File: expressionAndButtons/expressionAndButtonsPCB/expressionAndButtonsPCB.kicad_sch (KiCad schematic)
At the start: 62 parts, among them J1 Alimentazione, J2 Input comandi, J3 OUTPUT C, J4 OUTPUT I, J5 OUTPUT III, J6 INPUT C-I-III, U2 ProMicro

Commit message: Progresso bottoniera
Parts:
- removed J2: Input comandi, TerminalBlock_Phoenix:TerminalBlock_Phoenix_MKDS-1,5-16_1x16_P5.00mm_Horizontal, symbol Connector_Generic:Conn_01x16
- removed J3: OUTPUT C, TerminalBlock_Phoenix:TerminalBlock_Phoenix_MKDS-1,5-16_1x16_P5.00mm_Horizontal, symbol Connector_Generic:Conn_01x16
- added J2, J3: Conn_01x12, TerminalBlock_Phoenix:TerminalBlock_Phoenix_MPT-0,5-12-2.54_1x12_P2.54mm_Horizontal, symbol Connector_Generic:Conn_01x12
- added J7, J8: Conn_01x04, TerminalBlock_Phoenix:TerminalBlock_Phoenix_MPT-0,5-4-2.54_1x04_P2.54mm_Horizontal, symbol Connector_Generic:Conn_01x04
- J4, J5: footprint TerminalBlock_Phoenix:TerminalBlock_Phoenix_MKDS-1,5-9-5.08_1x09_P5.08mm_Horizontal -> TerminalBlock_Phoenix:TerminalBlock_Phoenix_MPT-0,5-9-2.54_1x09_P2.54mm_Horizontal
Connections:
- net at IN1.5 (D6), R7.1: now also J2.7 (Pin_7)
- net at Cresc1.10 (~{SRCLR}), Cresc1.13 (~{OE}), Cresc1.16 (VCC)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: now also Cresc2.10 (~{SRCLR}), Cresc2.13 (~{OE}), Cresc2.16 (VCC)
- net at IN1.11 (D0), R1.1: now also J2.1 (Pin_1)
- net at IN2.12 (D1), R10.1: now also J2.10 (Pin_10)
- net at IN2.13 (D2), R11.1: now also J2.11 (Pin_11)
- net at IN2.14 (D3), R12.1: now also J2.12 (Pin_12)
- net at IN2.3 (D4), R13.1: now also J7.1 (Pin_1)
- net at IN2.4 (D5), R14.1: now also J7.2 (Pin_2)
- net at IN2.5 (D6), R15.1: now also J7.3 (Pin_3)
- net at IN2.6 (D7), R16.1: now also J7.4 (Pin_4)
- net at IN1.12 (D1), R2.1: now also J2.2 (Pin_2)
- net at IN1.13 (D2), R3.1: now also J2.3 (Pin_3)
- net at IN1.14 (D3), R4.1: now also J2.4 (Pin_4)
- net at IN1.3 (D4), R5.1: now also J2.5 (Pin_5)
- net at IN1.4 (D5), R6.1: now also J2.6 (Pin_6)
- net at IN1.6 (D7), R8.1: now also J2.8 (Pin_8)
- net at IN2.11 (D0), R9.1: now also J2.9 (Pin_9)
- net at R17.2: now also J3.1 (Pin_1)
- net at R26.2: now also J3.10 (Pin_10)
- net at R27.2: now also J3.11 (Pin_11)
- net at R28.2: now also J3.12 (Pin_12)
- net at R29.2: now also J8.1 (Pin_1)
- net at R30.2: now also J8.2 (Pin_2)
- net at R31.2: now also J8.3 (Pin_3)
- net at R32.2: now also J8.4 (Pin_4)
- net at R18.2: now also J3.2 (Pin_2)
- net at R19.2: now also J3.3 (Pin_3)
- net at R20.2: now also J3.4 (Pin_4)
- net at R21.2: now also J3.5 (Pin_5)
- net at R22.2: now also J3.6 (Pin_6)
- net at R23.2: now also J3.7 (Pin_7)
- net at R24.2: now also J3.8 (Pin_8)
- net at R25.2: now also J3.9 (Pin_9)
- net at IN1.7 (~{Q7}): no longer IN2.10 (DS)
- net at IN1.9 (Q7): now also IN2.10 (DS)

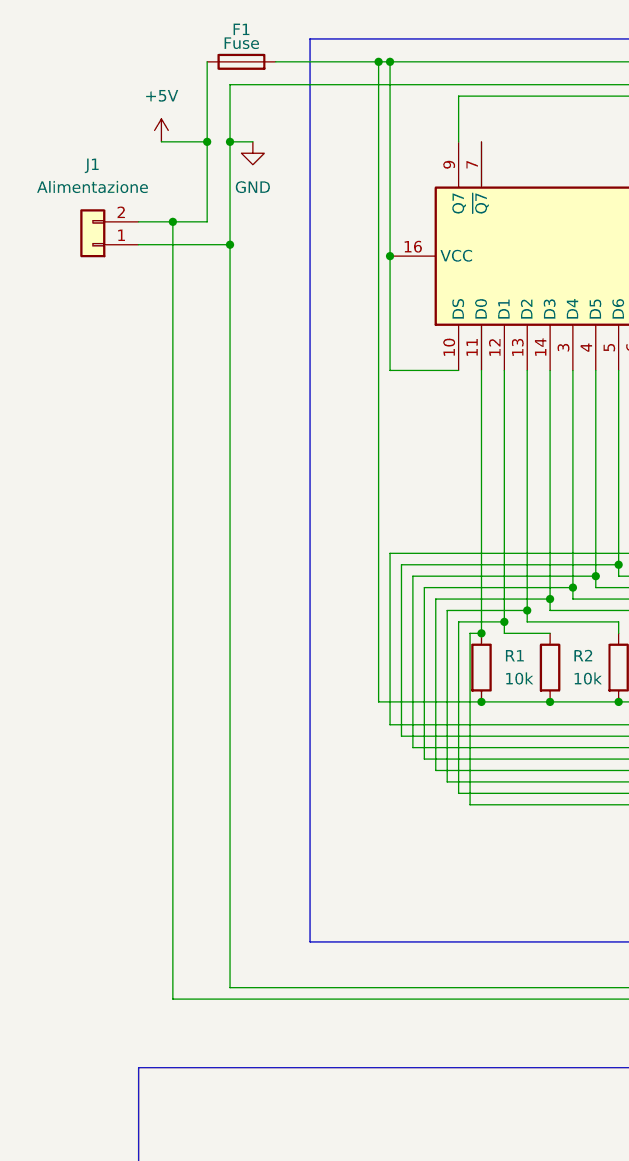
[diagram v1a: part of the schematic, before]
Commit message: First version buttons
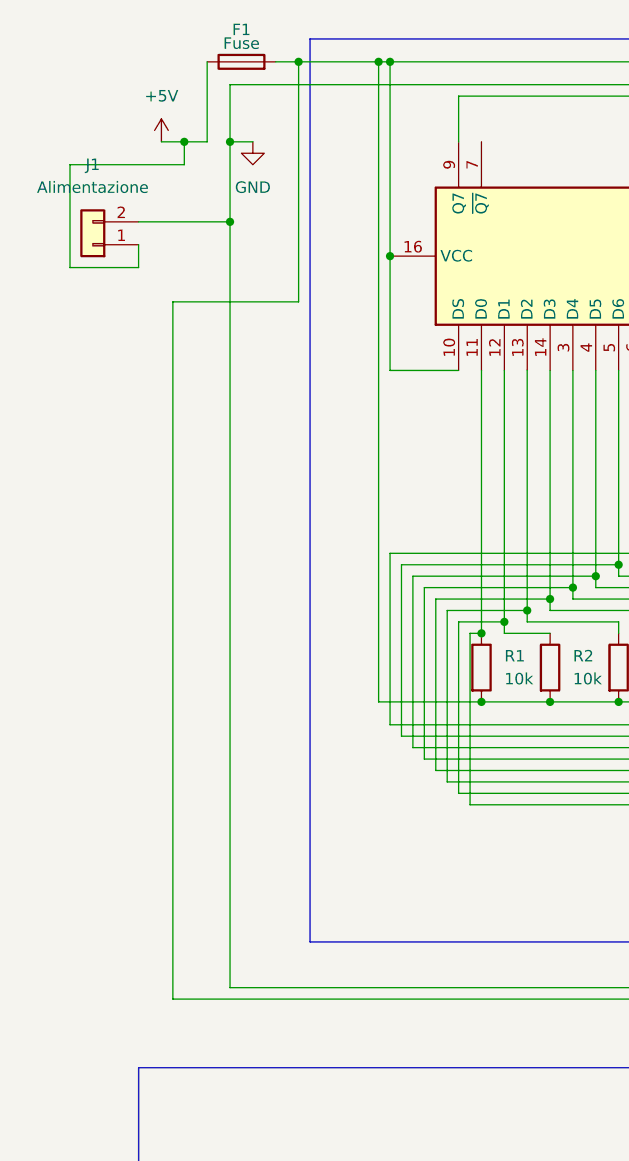
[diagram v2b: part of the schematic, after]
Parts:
- J6: footprint TerminalBlock_Phoenix:TerminalBlock_Phoenix_MKDS-1,5-5-5.08_1x05_P5.08mm_Horizontal -> TerminalBlock_Phoenix:TerminalBlock_Phoenix_MPT-0,5-5-2.54_1x05_P2.54mm_Horizontal
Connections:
- net +5V: now also J1.1 (Pin_1); no longer J1.2 (Pin_2), J6.4 (Pin_4)
- net GND: now also J1.2 (Pin_2); no longer J1.1 (Pin_1)
- net at Cresc1.10 (~{SRCLR}), Cresc1.13 (~{OE}), Cresc1.16 (VCC)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: now also J6.4 (Pin_4)
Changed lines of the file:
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@@
 	)
 	(junction
-		(at 29.21 34.29)
-		(diameter 0)
-		(color 0 0 0 0)
-	)
-	(junction
-		(at 35.56 36.83)
-		(diameter 0)
-		(color 0 0 0 0)
-	)
-	(junction
 		(at 111.76 16.51)
 		(diameter 0)
@@
 	)
 	(junction
-		(at 33.02 25.4)
-		(diameter 0)
-		(color 0 0 0 0)
-	)
-	(junction
 		(at 66.04 78.74)
 		(diameter 0)
@@
 	)
 	(junction
+		(at 35.56 34.29)
+		(diameter 0)
+		(color 0 0 0 0)
+	)
+	(junction
 		(at 236.22 116.84)
 		(diameter 0)
@@
 	)
 	(junction
+		(at 30.48 25.4)
+		(diameter 0)
+		(color 0 0 0 0)
+	)
+	(junction
 		(at 81.28 71.12)
 		(diameter 0)
@@
 	)
 	(junction
+		(at 43.18 16.51)
+		(diameter 0)
+		(color 0 0 0 0)
+	)
+	(junction
 		(at 132.08 87.63)
 		(diameter 0)
@@
 	(wire
 		(pts
+			(xy 43.18 43.18) (xy 43.18 16.51)
+		)
+		(stroke
+			(width 0)
+			(type default)
+		)
+	)
+	(wire
+		(pts
 			(xy 345.44 158.75) (xy 345.44 148.59)
 		)
@@
 	(wire
 		(pts
-			(xy 35.56 36.83) (xy 35.56 25.4)
+			(xy 254 72.39) (xy 254 83.82)
 		)
 		(stroke
@@
 	(wire
 		(pts
-			(xy 254 72.39) (xy 254 83.82)
+			(xy 259.08 154.94) (xy 278.13 154.94)
 		)
 		(stroke
@@
 	(wire
 		(pts
-			(xy 259.08 154.94) (xy 278.13 154.94)
+			(xy 147.32 87.63) (xy 154.94 87.63)
 		)
 		(stroke
@@
 	(wire
 		(pts
-			(xy 147.32 87.63) (xy 154.94 87.63)
+			(xy 312.42 83.82) (xy 312.42 77.47)
 		)
 		(stroke
@@
 	(wire
 		(pts
-			(xy 312.42 83.82) (xy 312.42 77.47)
+			(xy 30.48 27.94) (xy 17.78 27.94)
 		)
 		(stroke
@@
 	(wire
 		(pts
+			(xy 43.18 16.51) (xy 52.07 16.51)
+		)
+		(stroke
+			(width 0)
+			(type default)
+		)
+	)
+	(wire
+		(pts
 			(xy 341.63 184.15) (xy 354.33 184.15)
 		)
@@
 	(wire
 		(pts
+			(xy 17.78 39.37) (xy 25.4 39.37)
+		)
+		(stroke
+			(width 0)
+			(type default)
+		)
+	)
+	(wire
+		(pts
 			(xy 274.32 123.19) (xy 237.49 123.19)
 		)
@@
 	(wire
 		(pts
+			(xy 29.21 43.18) (xy 43.18 43.18)
+		)
+		(stroke
+			(width 0)
+			(type default)
+		)
+	)
+	(wire
+		(pts
 			(xy 73.66 76.2) (xy 93.98 76.2)
 		)
@@
 	(wire
 		(pts
-			(xy 91.44 50.8) (xy 91.44 57.15)
+			(xy 30.48 25.4) (xy 33.02 25.4)
 		)
 		(stroke
@@
 	(wire
 		(pts
-			(xy 369.57 184.15) (xy 389.89 184.15)
+			(xy 91.44 50.8) (xy 91.44 57.15)
 		)
 		(stroke
@@
 	(wire
 		(pts
-			(xy 360.68 59.69) (xy 360.68 64.77)
+			(xy 369.57 184.15) (xy 389.89 184.15)
 		)
 		(stroke
@@
 	(wire
 		(pts
-			(xy 53.34 16.51) (xy 53.34 38.1)
+			(xy 360.68 59.69) (xy 360.68 64.77)
 		)
 		(stroke
@@
 	(wire
 		(pts
-			(xy 25.4 34.29) (xy 29.21 34.29)
+			(xy 53.34 16.51) (xy 53.34 38.1)
 		)
 		(stroke
@@
 	(wire
 		(pts
-			(xy 25.4 36.83) (xy 35.56 36.83)
+			(xy 29.21 43.18) (xy 29.21 120.65)
 		)
 		(stroke
@@
 	(wire
 		(pts
+			(xy 25.4 39.37) (xy 25.4 36.83)
+		)
+		(stroke
+			(width 0)
+			(type default)
+		)
+	)
+	(wire
+		(pts
 			(xy 127 96.52) (xy 158.75 96.52)
 		)
@@
 	(wire
 		(pts
-			(xy 27.94 25.4) (xy 33.02 25.4)
+			(xy 27.94 25.4) (xy 30.48 25.4)
 		)
 		(stroke
@@
 	(wire
 		(pts
-			(xy 33.02 25.4) (xy 33.02 34.29)
-		)
-		(stroke
-			(width 0)
-			(type default)
-		)
-	)
-	(wire
-		(pts
 			(xy 59.69 77.47) (xy 68.58 77.47)
 		)
@@
 	(wire
 		(pts
+			(xy 30.48 25.4) (xy 30.48 27.94)
+		)
+		(stroke
+			(width 0)
+			(type default)
+		)
+	)
+	(wire
+		(pts
 			(xy 57.15 74.93) (xy 73.66 74.93)
 		)
@@
 	(wire
 		(pts
-			(xy 35.56 119.38) (xy 35.56 36.83)
+			(xy 35.56 25.4) (xy 35.56 34.29)
 		)
 		(stroke
@@
 	(wire
 		(pts
-			(xy 29.21 34.29) (xy 29.21 120.65)
-		)
-		(stroke
-			(width 0)
-			(type default)
-		)
-	)
-	(wire
-		(pts
 			(xy 60.96 20.32) (xy 110.49 20.32)
 		)
@@
 	(wire
 		(pts
-			(xy 40.64 16.51) (xy 52.07 16.51)
+			(xy 40.64 16.51) (xy 43.18 16.51)
 		)
 		(stroke
@@
 	(wire
 		(pts
+			(xy 35.56 34.29) (xy 35.56 119.38)
+		)
+		(stroke
+			(width 0)
+			(type default)
+		)
+	)
+	(wire
+		(pts
 			(xy 160.02 52.07) (xy 152.4 52.07)
 		)
@@
 	(wire
 		(pts
-			(xy 29.21 34.29) (xy 33.02 34.29)
+			(xy 17.78 27.94) (xy 17.78 39.37)
 		)
 		(stroke
@@
 	(wire
 		(pts
+			(xy 25.4 34.29) (xy 35.56 34.29)
+		)
+		(stroke
+			(width 0)
+			(type default)
+		)
+	)
+	(wire
+		(pts
 			(xy 287.02 153.67) (xy 287.02 163.83)
 		)
@@
 			)
 		)
-		(property "Footprint" "TerminalBlock_Phoenix:TerminalBlock_Phoenix_MKDS-1,5-5-5.08_1x05_P5.08mm_Horizontal"
+		(property "Footprint" "TerminalBlock_Phoenix:TerminalBlock_Phoenix_MPT-0,5-5-2.54_1x05_P2.54mm_Horizontal"
 			(at 139.7 231.14 0)
 			(effects

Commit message: update
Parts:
- J1: footprint TerminalBlock_Phoenix:TerminalBlock_Phoenix_MKDS-1,5-2-5.08_1x02_P5.08mm_Horizontal -> TerminalBlock_Phoenix:TerminalBlock_Phoenix_MPT-0,5-2-2.54_1x02_P2.54mm_Horizontal
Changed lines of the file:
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@@
 			)
 		)
-		(property "Footprint" "TerminalBlock_Phoenix:TerminalBlock_Phoenix_MKDS-1,5-2-5.08_1x02_P5.08mm_Horizontal"
+		(property "Footprint" "TerminalBlock_Phoenix:TerminalBlock_Phoenix_MPT-0,5-2-2.54_1x02_P2.54mm_Horizontal"
 			(at 20.32 36.83 0)
 			(effects

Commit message: problem fix
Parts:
- removed J2, J3: Conn_01x12, TerminalBlock_Phoenix:TerminalBlock_Phoenix_MPT-0,5-12-2.54_1x12_P2.54mm_Horizontal, symbol Connector_Generic:Conn_01x12
- removed J7, J8: Conn_01x04, TerminalBlock_Phoenix:TerminalBlock_Phoenix_MPT-0,5-4-2.54_1x04_P2.54mm_Horizontal, symbol Connector_Generic:Conn_01x04
- added J2, J7: Conn_01x06, TerminalBlock_Phoenix:TerminalBlock_Phoenix_MPT-0,5-6-2.54_1x06_P2.54mm_Horizontal, symbol Connector_Generic:Conn_01x06
- added J3, J9: Conn_01x10, TerminalBlock_Phoenix:TerminalBlock_Phoenix_MPT-0,5-10-2.54_1x10_P2.54mm_Horizontal, symbol Connector_Generic:Conn_01x10
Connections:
- net GND: now also Cresc1.13 (~{OE}), Cresc2.13 (~{OE}), E1.13 (~{OE}), E2.13 (~{OE})
- net at IN1.5 (D6), R7.1: now also J9.7 (Pin_7)
- net at Cresc1.10 (~{SRCLR}), Cresc1.16 (VCC), Cresc2.10 (~{SRCLR})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: no longer Cresc1.13 (~{OE}), Cresc2.13 (~{OE}), E1.13 (~{OE}), E2.13 (~{OE})
- net at IN2.12 (D1), R10.1: now also J9.10 (Pin_10)
- net at R30.2: now also J7.4 (Pin_4)
- net at R22.2: now also J3.6 (Pin_6)
- net at R17.2: now also J3.1 (Pin_1)
- net at R26.2: now also J3.10 (Pin_10)
- net at R27.2: now also J7.1 (Pin_1)
- net at R28.2: now also J7.2 (Pin_2)
- net at R18.2: now also J3.2 (Pin_2)
- net at R19.2: now also J3.3 (Pin_3)
- net at R20.2: now also J3.4 (Pin_4)
- net at R21.2: now also J3.5 (Pin_5)
- net at R23.2: now also J3.7 (Pin_7)
- net at R24.2: now also J3.8 (Pin_8)
- net at R25.2: now also J3.9 (Pin_9)
- net at IN2.3 (D4), R13.1: now also J2.3 (Pin_3)
- net at IN1.12 (D1), R2.1: now also J9.2 (Pin_2)
- net at IN2.4 (D5), R14.1: now also J2.4 (Pin_4)
- net at IN2.14 (D3), R12.1: now also J2.2 (Pin_2)
- net at IN2.6 (D7), R16.1: now also J2.6 (Pin_6)
- net at IN2.5 (D6), R15.1: now also J2.5 (Pin_5)
- net at R32.2: now also J7.6 (Pin_6)
- net at IN1.11 (D0), R1.1: now also J9.1 (Pin_1)
- net at IN2.13 (D2), R11.1: now also J2.1 (Pin_1)
- net at IN1.13 (D2), R3.1: now also J9.3 (Pin_3)
- net at IN1.14 (D3), R4.1: now also J9.4 (Pin_4)
- net at IN1.3 (D4), R5.1: now also J9.5 (Pin_5)
- net at IN1.4 (D5), R6.1: now also J9.6 (Pin_6)
- net at IN1.6 (D7), R8.1: now also J9.8 (Pin_8)
- net at IN2.11 (D0), R9.1: now also J9.9 (Pin_9)
- net at R29.2: now also J7.3 (Pin_3)
- net at R31.2: now also J7.5 (Pin_5)
